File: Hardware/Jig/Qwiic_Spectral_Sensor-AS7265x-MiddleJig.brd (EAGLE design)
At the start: 35.6 x 40.6 mm, 93 parts, among them J2 Serial Interface, J5 Flash Programming, J8 PTH, U1 AS72651, U3 4MB Flash, U5 AS72653, U6 AS72652

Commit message: Silk changes before panelization
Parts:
- removed U$1, U$36, U$37: (no value), buzzard_labels (7):#0
- removed U$38, U$39, U$40: (no value), buzzard_labels (7):#1
- added E$1, E$2, E$3, E$4: (no value), SparkFun-Hardware:STAND-OFF-TIGHT
- added E$5, E$6: (no value), SparkFun-Hardware:NUBBIN_LOCKER
- D2: device SparkFun-LED:SUPER_BRIGHT_SMD_LED_3014 -> SparkX:SUPER_BRIGHT_SMD_LED_1206
- moved U$10 67.4 mm to (92.1, 31.8)
- moved FRAME1 67.3 mm to (55.9, -30.5)
- moved LOGO4 67.3 mm to (100.3, 2.54)
- moved U$11 67.3 mm to (68.2, 5.59)
- moved U$13 67.3 mm to (78.4, 7.87)
- moved U$17 67.3 mm to (78.7, 33.9)
- moved U$19 67.3 mm to (91.4, 34.8)
- moved U$2 67.3 mm to (72.9, 32.5)
- moved U$21 67.3 mm to (85.2, 34.4)
- moved U$22 67.3 mm to (88.6, 33.0)
- moved U$25 67.3 mm to (91.4, 1.65)
- moved U$26 67.3 mm to (86.4, 1.65)
- moved U$29 67.3 mm to (78.7, 1.52)
- moved U$30 67.3 mm to (91.4, 1.65)
- moved U$32 67.3 mm to (86.4, 1.65)
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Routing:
- net 3.3V: track 143.3 -> 0.00 mm, vias 4 -> 0
- net RX/SCL: track 99.0 -> 0.00 mm, vias 6 -> 0
- net TX/SDA: track 93.2 -> 0.00 mm, vias 5 -> 0
- net SDA_S: track 56.9 -> 0.00 mm, vias 3 -> 0
- net SCL_S: track 56.2 -> 0.00 mm, vias 3 -> 0
- net !RST: track 50.8 -> 0.00 mm, vias 3 -> 0
- net !INT: track 30.2 -> 0.00 mm, vias 1 -> 0
- net LED_DRV: track 21.0 -> 0.00 mm, vias 1 -> 0
- net !CS_EE: track 17.6 -> 0.00 mm, vias 2 -> 0
- net I2C_ENB: track 16.8 -> 0.00 mm, vias 1 -> 0
- net MISO: track 15.5 -> 0.00 mm, vias 1 -> 0
- net !RST-ADDR: track 14.9 -> 0.00 mm, vias 2 -> 0
- net N$2: track 11.8 -> 0.00 mm, vias 2 -> 0
- net MOSI: track 9.65 -> 0.00 mm
- net LED_DRV1: track 9.51 -> 0.00 mm
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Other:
- board size 35.6 x 40.6 mm -> 48.3 x 53.3 mm
- board text added: "#6"
- board text added: "6"
- board text added: "DEV-Me"
- board text added: "GPS-Test"

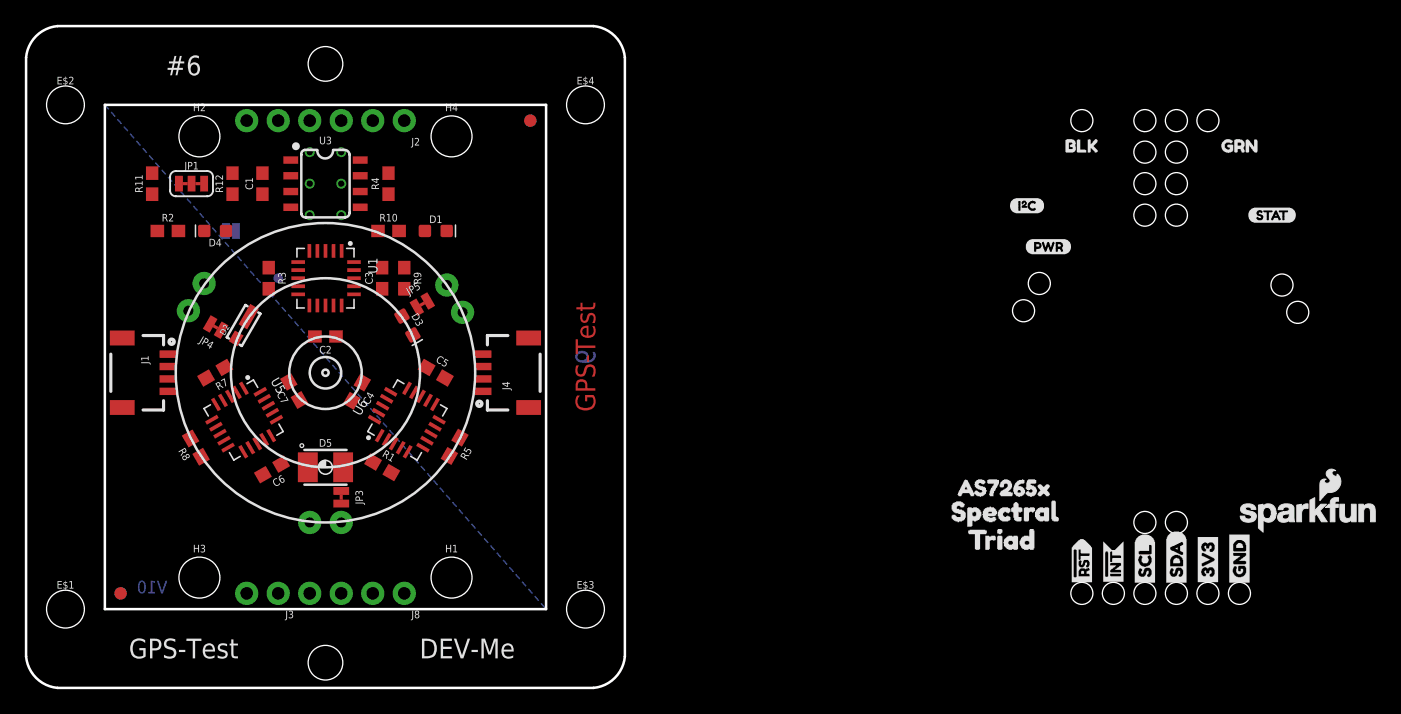
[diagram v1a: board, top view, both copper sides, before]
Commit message: Intermediate committ. Probably ignore the jig files.
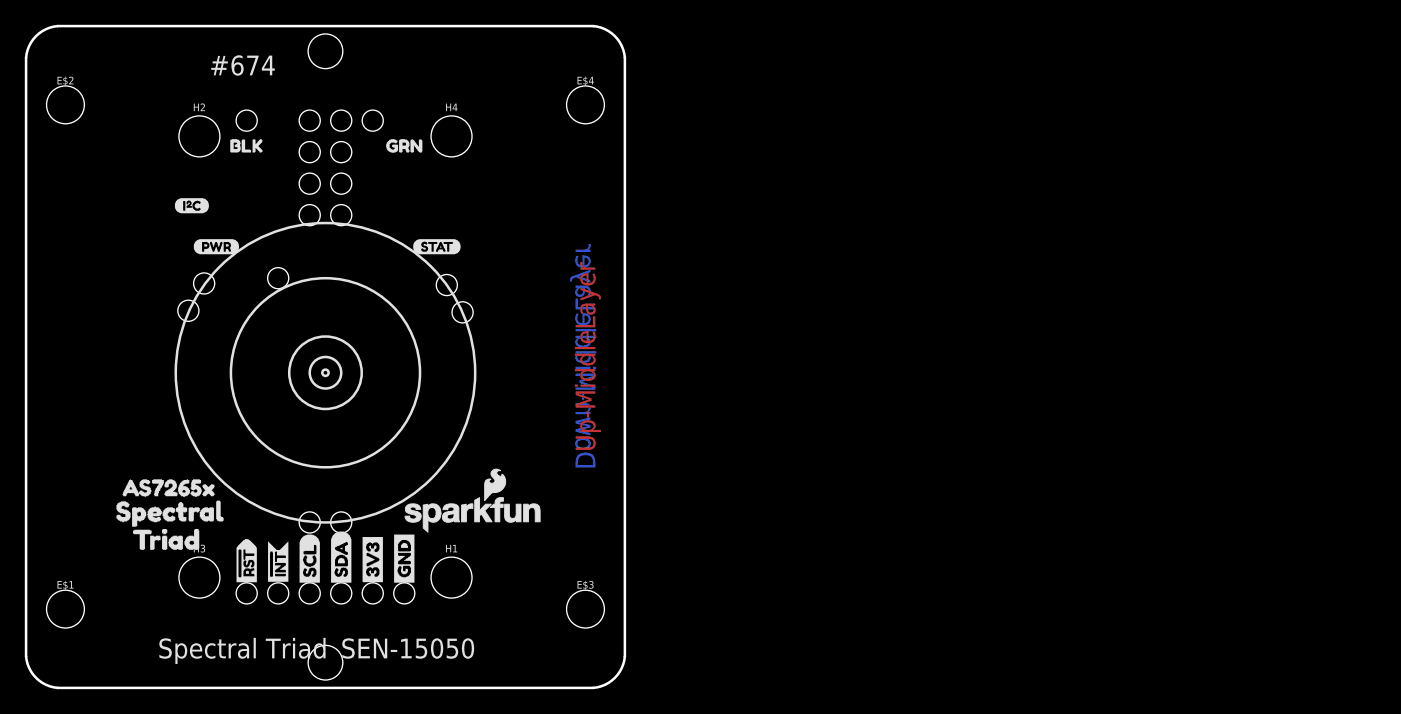
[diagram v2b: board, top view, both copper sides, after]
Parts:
- removed BULB1, BULB2, BULB3: (no value), SparkX:LED_5MM_NOSILK
- removed C1: 1.0uF, SparkFun-Capacitors:0603
- removed C2, C4, C6: 0.1uF, SparkFun-Capacitors:0603
- removed C3, C5, C7: 10uF, SparkFun-Capacitors:0603
- removed D1: BLUE, SparkFun-LED:LED-0603
- removed D2: 5700k, SparkX:SUPER_BRIGHT_SMD_LED_1206
- removed D3: IR, SparkFun-LED:LED-0603
- removed D4: RED, SparkFun-LED:LED-0603
- removed D5: UV, SparkFun-LED:PLCC-2
- removed FD1, FD2, FD3, FD4: FIDUCIAL1X2, SparkFun-Aesthetics:FIDUCIAL-1X2
- removed J1, J4: (no value), SparkFun-Connectors:1X04_1MM_RA
- removed J2: Serial Interface, SparkFun-Connectors:1X06_NO_SILK
- removed J3: (no value), SparkFun-Connectors:1X02_NO_SILK
- removed J5: Flash Programming, SparkFun-Connectors:2X3_TEST_POINTS
- removed J8: PTH, SparkFun-Connectors:1X04_NO_SILK
- removed JP1: (no value), SparkFun-Jumpers:SMT-JUMPER_3_2-NC_TRACE_SILK
- removed JP2: (no value), SparkFun-Jumpers:SMT-JUMPER_2_NO_SILK
- removed JP3, JP4, JP5: (no value), SparkFun-Jumpers:SMT-JUMPER_2_NC_TRACE_NO-SILK
- removed R1, R3, R4, R5, R7, R8: 10k, SparkFun-Resistors:0603
- removed R10, R11, R12, R9: 2.2k, SparkFun-Resistors:0603
- removed R2: 1k, SparkFun-Resistors:0603
- removed TP1: (no value), SparkFun-Connectors:PAD.03X.03
- removed U1: AS72651, Qwiic_Spectral_Sensor-AS7265x:LGA20
- removed U3: 4MB Flash, SparkFun-IC-Memory:SO08
- removed U5: AS72653, Qwiic_Spectral_Sensor-AS7265x:LGA20
- removed U6: AS72652, Qwiic_Spectral_Sensor-AS7265x:LGA20
- added U$1, U$36, U$37: (no value), buzzard_labels (7):#0
- added U$38, U$39, U$40: (no value), buzzard_labels (7):#1
- moved U$10 67.4 mm to (24.8, 29.2)
- moved LOGO4 67.3 mm to (33.0, 2.54)
- moved U$11 67.3 mm to (0.89, 5.59)
- moved U$13 67.3 mm to (11.0, 7.87)
- moved U$17 67.3 mm to (11.4, 33.9)
- moved U$19 67.3 mm to (24.1, 34.8)
- moved U$2 67.3 mm to (5.59, 32.5)
- moved U$21 67.3 mm to (17.9, 34.4)
- moved U$22 67.3 mm to (21.3, 33.0)
- moved U$25 67.3 mm to (24.1, 1.65)
- moved U$26 67.3 mm to (19.1, 1.65)
- moved U$29 67.3 mm to (11.4, 1.52)
- moved U$30 67.3 mm to (24.1, 1.65)
- moved U$32 67.3 mm to (19.1, 1.65)
- moved U$35 67.3 mm to (11.4, 1.52)
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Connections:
- removed net !CS_EE: J5.5, U1.6, U3.1
- removed net !INT: J3.1, U1.9
- removed net !RST: J3.2, R4.1, U1.2, U5.2
- removed net !RST-ADDR: U1.13, U6.2
- removed net 3.3V: BULB1.A, BULB2.A, BULB3.A, C1.1, C2.1, C3.1, C4.1, C5.1, C6.1, C7.1, D1.A, D4.A, J1.2, J2.4, J4.2, J5.2, J8.2, JP1.2, JP3.2, JP4.2, JP5.2, R10.2, R3.2, R4.2, R9.2, U1.14, U1.17, U3.3, U3.7, U3.8, U5.14, U5.17, U6.14, U6.17
- removed net GND: C1.2, C2.2, C3.2, C4.2, C5.2, C6.2, C7.2, J1.1, J2.6, J4.1, J5.6, J8.1, JP2.1, R1.1, R2.1, R5.1, R7.1, R8.1, U1.16, U3.4, U5.16, U6.16
- removed net I2C_ENB: JP2.2, R3.1, TP1.P$1, U1.8
- removed net LED_DRV: BULB1.K, D2.C, U1.15
- removed net LED_DRV1: BULB2.K, D3.C, U6.15
- removed net LED_DRV2: BULB3.K, D5.C, U5.15
- removed net MISO: J5.1, U1.5, U3.2
- removed net MOSI: J5.4, U1.4, U3.5
- removed net N$1: D4.C, R2.2
- removed net N$11: D5.A, JP3.1
- removed net N$12: R8.2, U5.7
- removed net N$13: R7.2, U5.5
- removed net N$2: D1.C, U1.18
- removed net N$3: R5.2, U6.7
- removed net N$4: JP1.3, R12.2
- removed net N$5: JP1.1, R11.2
- removed net N$6: D2.A, JP4.1
- removed net N$8: D3.A, JP5.1
- removed net N$9: R1.2, U6.5
- removed net RX/SCL: J1.4, J2.3, J4.4, J8.4, R11.1, U1.11
- removed net SCK: J5.3, U1.3, U3.6
- removed net SCL_S: R9.1, U1.20, U5.9, U6.9
- removed net SDA_S: R10.1, U1.1, U5.10, U6.10
- removed net TX/SDA: J1.3, J2.2, J4.3, J8.3, R12.1, U1.12
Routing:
- removed copper zone on layer 1, net GND
- removed copper zone on layer 16, net GND
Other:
- outline, holes or cut-outs redrawn
- board text added: "#674"
- board text added: "Down-MiddleLayer"
- board text added: "SEN-15050"
- board text added: "Spectral Triad"
- board text added: "Up-MiddleLayer"
- board text removed: "#6"
- board text removed: "6"
- board text removed: "DEV-Me"
- board text removed: "GPS-Test"
- board text removed: "V10"
